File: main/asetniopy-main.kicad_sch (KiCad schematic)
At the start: 19 parts, among them J1 Conn_01x02, J2 Conn_01x02, J3 Conn_01x02, J4 Conn_01x02, J5 Conn_01x02, J6 Power/Reset, J7 BAT+, J8 BAT-, U1 ProMicro, U2 LIS2DW12

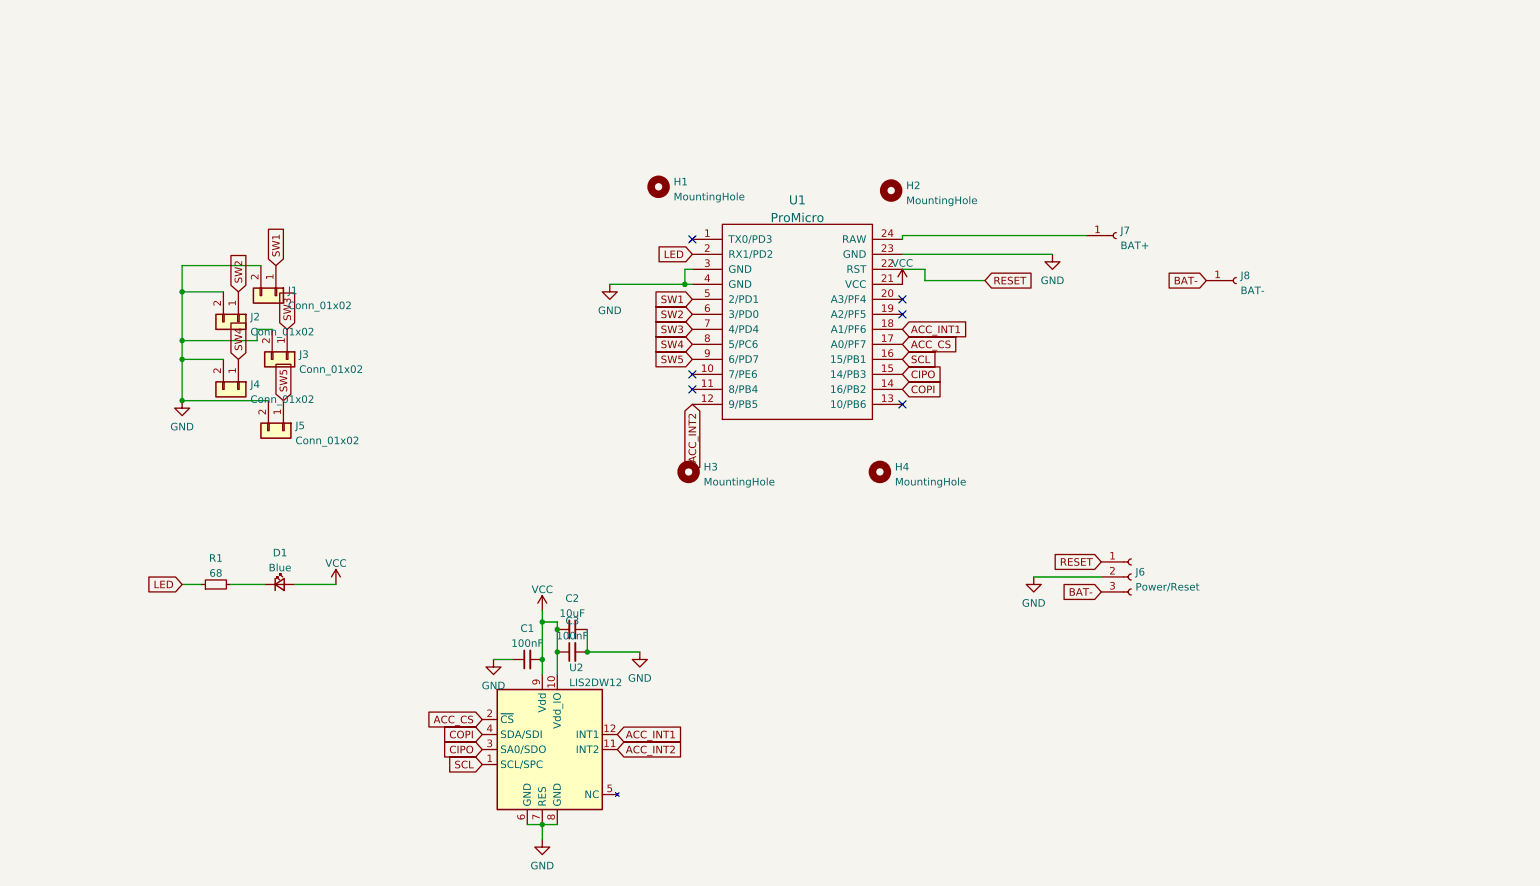
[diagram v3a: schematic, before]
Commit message: Switch to RGB LED.
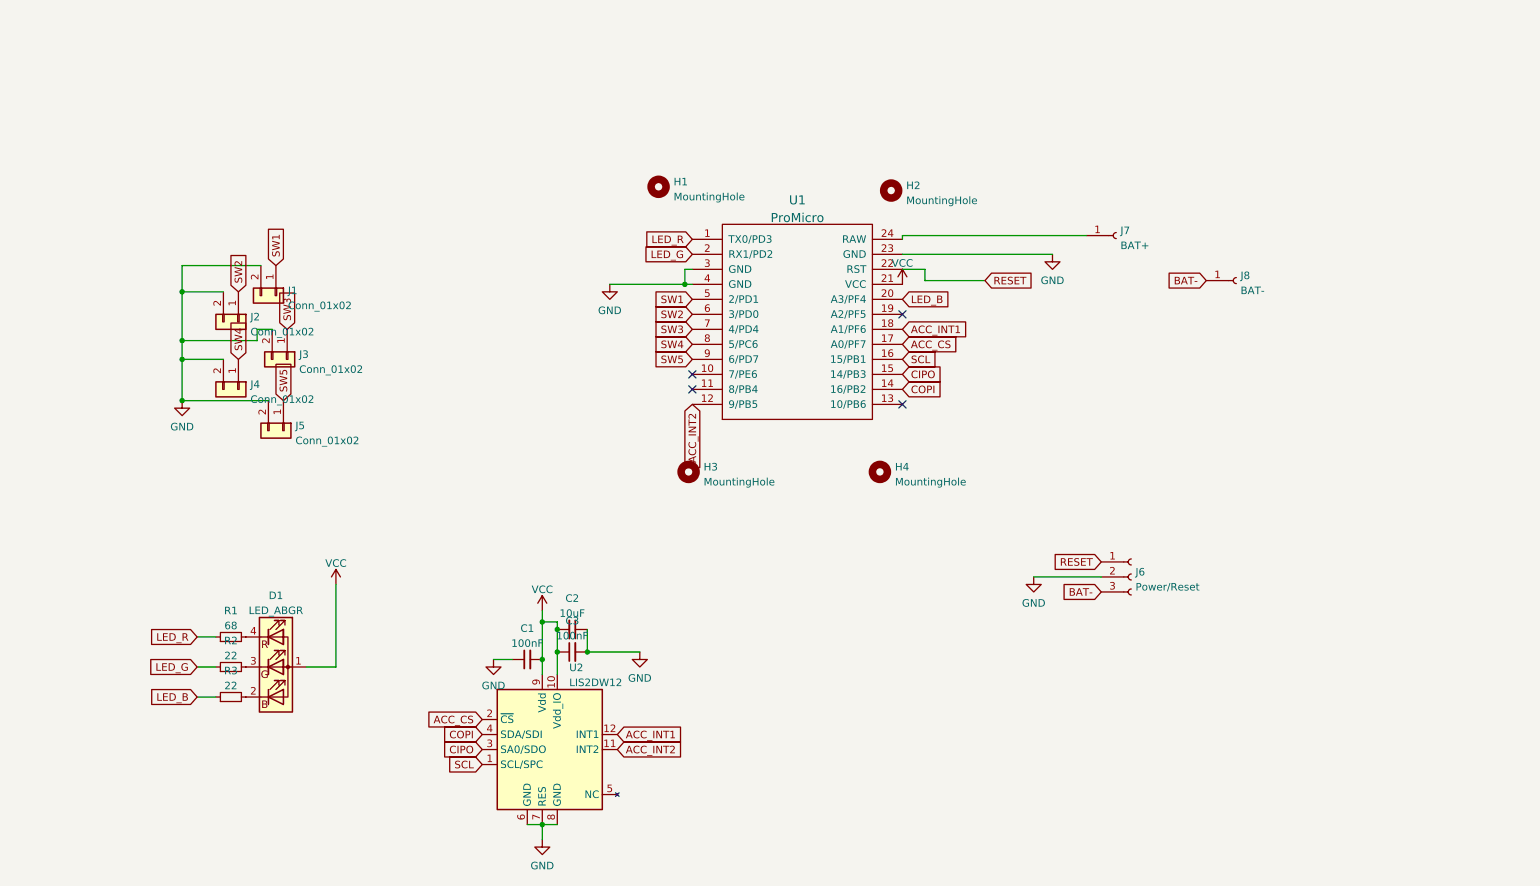
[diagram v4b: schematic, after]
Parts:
- removed D1: Blue, LED_SMD:LED_0603_1608Metric, symbol Device:LED_Small
- added D1: LED_ABGR, LED_SMD:LED_RGB_Wuerth-PLCC4_3.2x2.8mm_150141M173100, symbol Device:LED_ABGR
- added R2, R3: 22, Resistor_SMD:R_0603_1608Metric, symbol Device:R_Small
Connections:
- net VCC: now also D1.1 (A)
- net at R1.2: now also D1.4 (RK)
- net LED_R: now reaches U1.1 (TX0/PD3)
- net LED_R: now also R1.1
- net LED_B: now reaches U1.20 (A3/PF4)
- net LED_B: now also R3.1
- net LED renamed LED_G
- net LED_G: now also R2.1; no longer R1.1
- new net: D1.2 (BK), R3.2
- new net: D1.3 (GK), R2.2
- no-connect marks 6 -> 4
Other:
- moved on the sheet: R1
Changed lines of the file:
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@@
   )
   (no_connect (at 172.085 74.93))
-  (no_connect (at 136.525 62.23))
   (no_connect (at 136.525 85.09))
   (no_connect (at 136.525 87.63))
   (no_connect (at 172.085 90.17))
-  (no_connect (at 172.085 72.39))
   (wire (pts (xy 50.165 82.55) (xy 50.165 89.535))
     (stroke (width 0) (type default) (color 0 0 0 0))
@@
     (stroke (width 0) (type default) (color 0 0 0 0))
   )
+  (wire (pts (xy 76.2 120.65) (xy 76.2 134.62))
+    (stroke (width 0) (type default) (color 0 0 0 0))
+  )
   (wire (pts (xy 50.165 82.55) (xy 57.15 82.55))
     (stroke (width 0) (type default) (color 0 0 0 0))
@@
     (stroke (width 0) (type default) (color 0 0 0 0))
   )
+  (wire (pts (xy 52.705 139.7) (xy 55.88 139.7))
+    (stroke (width 0) (type default) (color 0 0 0 0))
+  )
   (wire (pts (xy 111.125 161.29) (xy 111.125 163.83))
     (stroke (width 0) (type default) (color 0 0 0 0))
@@
     (stroke (width 0) (type default) (color 0 0 0 0))
   )
+  (wire (pts (xy 52.705 134.62) (xy 55.88 134.62))
+    (stroke (width 0) (type default) (color 0 0 0 0))
+  )
   (wire (pts (xy 136.525 67.31) (xy 135.255 67.31))
     (stroke (width 0) (type default) (color 0 0 0 0))
@@
     (stroke (width 0) (type default) (color 0 0 0 0))
   )
-  (wire (pts (xy 69.215 120.65) (xy 76.2 120.65))
-    (stroke (width 0) (type default) (color 0 0 0 0))
-  )
   (wire (pts (xy 50.165 79.375) (xy 62.865 79.375))
     (stroke (width 0) (type default) (color 0 0 0 0))
@@
     (stroke (width 0) (type default) (color 0 0 0 0))
   )
-  (wire (pts (xy 50.165 120.65) (xy 53.34 120.65))
-    (stroke (width 0) (type default) (color 0 0 0 0))
-  )
-  (wire (pts (xy 58.42 120.65) (xy 64.135 120.65))
+  (wire (pts (xy 52.705 129.54) (xy 55.88 129.54))
+    (stroke (width 0) (type default) (color 0 0 0 0))
+  )
+  (wire (pts (xy 76.2 134.62) (xy 71.12 134.62))
     (stroke (width 0) (type default) (color 0 0 0 0))
   )
@@
     )
   )
+  (global_label "LED_B" (shape input) (at 52.705 139.7 180) (fields_autoplaced)
+    (effects (font (size 1.27 1.27)) (justify right))
+    (property "Intersheet References" "${INTERSHEET_REFS}" (id 0) (at 44.6071 139.6206 0)
+      (effects (font (size 1.27 1.27)) (justify right) hide)
+    )
+  )
   (global_label "BAT-" (shape input) (at 223.52 69.215 180) (fields_autoplaced)
     (effects (font (size 1.27 1.27)) (justify right))
@@
     )
   )
-  (global_label "LED" (shape input) (at 136.525 64.77 180) (fields_autoplaced)
-    (effects (font (size 1.27 1.27)) (justify right))
-    (property "Intersheet References" "${INTERSHEET_REFS}" (id 0) (at 130.6648 64.6906 0)
+  (global_label "LED_G" (shape input) (at 136.525 64.77 180) (fields_autoplaced)
+    (effects (font (size 1.27 1.27)) (justify right))
+    (property "Intersheet References" "${INTERSHEET_REFS}" (id 0) (at 128.4271 64.6906 0)
       (effects (font (size 1.27 1.27)) (justify right) hide)
     )
@@
     )
   )
+  (global_label "LED_B" (shape input) (at 172.085 72.39 0) (fields_autoplaced)
+    (effects (font (size 1.27 1.27)) (justify left))
+    (property "Intersheet References" "${INTERSHEET_REFS}" (id 0) (at 180.1829 72.3106 0)
+      (effects (font (size 1.27 1.27)) (justify left) hide)
+    )
+  )
   (global_label "SW3" (shape input) (at 136.525 77.47 180) (fields_autoplaced)
     (effects (font (size 1.27 1.27)) (justify right))
@@
     )
   )
+  (global_label "LED_R" (shape input) (at 136.525 62.23 180) (fields_autoplaced)
+    (effects (font (size 1.27 1.27)) (justify right))
+    (property "Intersheet References" "${INTERSHEET_REFS}" (id 0) (at 128.4271 62.1506 0)
+      (effects (font (size 1.27 1.27)) (justify right) hide)
+    )
+  )
+  (global_label "LED_G" (shape input) (at 52.705 134.62 180) (fields_autoplaced)
+    (effects (font (size 1.27 1.27)) (justify right))
+    (property "Intersheet References" "${INTERSHEET_REFS}" (id 0) (at 44.6071 134.5406 0)
+      (effects (font (size 1.27 1.27)) (justify right) hide)
+    )
+  )
   (global_label "SW3" (shape input) (at 67.945 77.47 90) (fields_autoplaced)
     (effects (font (size 1.27 1.27)) (justify left))
@@
     )
   )
-  (global_label "LED" (shape input) (at 50.165 120.65 180) (fields_autoplaced)
-    (effects (font (size 1.27 1.27)) (justify right))
-    (property "Intersheet References" "${INTERSHEET_REFS}" (id 0) (at 44.3048 120.7294 0)
-      (effects (font (size 1.27 1.27)) (justify right) hide)
-    )
-  )
-  (symbol (lib_id "Device:R_Small") (at 55.88 120.65 90) (unit 1)
-    (in_bom yes) (on_board yes) (fields_autoplaced)
-    (property "Reference" "R1" (id 0) (at 55.88 116.2136 90))
-    (property "Value" "68" (id 1) (at 55.88 118.7505 90))
-    (property "Footprint" "Resistor_SMD:R_0603_1608Metric" (id 2) (at 55.88 120.65 0)
-      (effects (font (size 1.27 1.27)) hide)
-    )
-    (property "Datasheet" "~" (id 3) (at 55.88 120.65 0)
-      (effects (font (size 1.27 1.27)) hide)
-    )
-    (property "LCSC Part Number" "C27592" (id 4) (at 55.88 120.65 90)
+  (global_label "LED_R" (shape input) (at 52.705 129.54 180) (fields_autoplaced)
+    (effects (font (size 1.27 1.27)) (justify right))
+    (property "Intersheet References" "${INTERSHEET_REFS}" (id 0) (at 44.6071 129.4606 0)
+      (effects (font (size 1.27 1.27)) (justify right) hide)
+    )
+  )
+  (symbol (lib_id "Device:R_Small") (at 58.42 129.54 90) (unit 1)
+    (in_bom yes) (on_board yes) (fields_autoplaced)
+    (property "Reference" "R1" (id 0) (at 58.42 125.1036 90))
+    (property "Value" "68" (id 1) (at 58.42 127.6405 90))
+    (property "Footprint" "Resistor_SMD:R_0603_1608Metric" (id 2) (at 58.42 129.54 0)
+      (effects (font (size 1.27 1.27)) hide)
+    )
+    (property "Datasheet" "~" (id 3) (at 58.42 129.54 0)
+      (effects (font (size 1.27 1.27)) hide)
+    )
+    (property "LCSC Part Number" "C27592" (id 4) (at 58.42 129.54 90)
       (effects (font (size 1.27 1.27)) hide)
     )
@@
       (effects (font (size 1.27 1.27)) hide)
     )
+  )
+  (symbol (lib_id "Device:R_Small") (at 58.42 139.7 90) (unit 1)
+    (in_bom yes) (on_board yes) (fields_autoplaced)
+    (property "Reference" "R3" (id 0) (at 58.42 135.2636 90))
+    (property "Value" "22" (id 1) (at 58.42 137.8005 90))
+    (property "Footprint" "Resistor_SMD:R_0603_1608Metric" (id 2) (at 58.42 139.7 0)
+      (effects (font (size 1.27 1.27)) hide)
+    )
+    (property "Datasheet" "~" (id 3) (at 58.42 139.7 0)
+      (effects (font (size 1.27 1.27)) hide)
+    )
+    (property "LCSC Part Number" "C25092" (id 4) (at 58.42 139.7 90)
+      (effects (font (size 1.27 1.27)) hide)
+    )
+    (pin "1")
+    (pin "2")
   )
   (symbol (lib_id "power:VCC") (at 76.2 120.65 0) (unit 1)
@@
     (pin "9")
   )
+  (symbol (lib_id "Device:LED_ABGR") (at 66.04 134.62 0) (unit 1)
+    (in_bom yes) (on_board yes) (fields_autoplaced)
+    (property "Reference" "D1" (id 0) (at 66.04 122.5382 0))
+    (property "Value" "LED_ABGR" (id 1) (at 66.04 125.0751 0))
+    (property "Footprint" "LED_SMD:LED_RGB_Wuerth-PLCC4_3.2x2.8mm_150141M173100" (id 2) (at 66.04 135.89 0)
+      (effects (font (size 1.27 1.27)) hide)
+    )
+    (property "Datasheet" "~" (id 3) (at 66.04 135.89 0)
+      (effects (font (size 1.27 1.27)) hide)
+    )
+    (property "LCSC Part Number" "C409779" (id 4) (at 66.04 134.62 0)
+      (effects (font (size 1.27 1.27)) hide)
+    )
+    (pin "1")
+    (pin "2")
+    (pin "3")
+    (pin "4")
+  )
   (symbol (lib_id "power:GND") (at 50.165 89.535 0) (unit 1)
     (in_bom yes) (on_board yes) (fields_autoplaced)
@@
       (effects (font (size 1.27 1.27)) hide)
     )
-  )
-  (symbol (lib_id "Device:LED_Small") (at 66.675 120.65 0) (unit 1)
-    (in_bom yes) (on_board yes) (fields_autoplaced)
-    (property "Reference" "D1" (id 0) (at 66.7385 115.2992 0))
-    (property "Value" "Blue" (id 1) (at 66.7385 117.8361 0))
-    (property "Footprint" "LED_SMD:LED_0603_1608Metric" (id 2) (at 66.675 120.65 90)
-      (effects (font (size 1.27 1.27)) hide)
-    )
-    (property "Datasheet" "~" (id 3) (at 66.675 120.65 90)
-      (effects (font (size 1.27 1.27)) hide)
-    )
-    (property "LCSC Part Number" "C72041" (id 4) (at 66.675 120.65 0)
-      (effects (font (size 1.27 1.27)) hide)
-    )
-    (pin "1")
-    (pin "2")
   )
   (symbol (lib_id "Device:C_Small") (at 108.585 133.35 90) (unit 1)
@@
     (pin "1")
   )
+  (symbol (lib_id "Device:R_Small") (at 58.42 134.62 90) (unit 1)
+    (in_bom yes) (on_board yes) (fields_autoplaced)
+    (property "Reference" "R2" (id 0) (at 58.42 130.1836 90))
+    (property "Value" "22" (id 1) (at 58.42 132.7205 90))
+    (property "Footprint" "Resistor_SMD:R_0603_1608Metric" (id 2) (at 58.42 134.62 0)
+      (effects (font (size 1.27 1.27)) hide)
+    )
+    (property "Datasheet" "~" (id 3) (at 58.42 134.62 0)
+      (effects (font (size 1.27 1.27)) hide)
+    )
+    (property "LCSC Part Number" "C25092" (id 4) (at 58.42 134.62 90)
+      (effects (font (size 1.27 1.27)) hide)
+    )
+    (pin "1")
+    (pin "2")
+  )
   (sheet_instances
     (path "/" (page "1"))
@@
       (reference "C3") (unit 1) (value "100nF") (footprint "Capacitor_SMD:C_0603_1608Metric")
     )
-    (path "/a3912c3b-a7ed-4069-b82c-93c869bd3701"
-      (reference "D1") (unit 1) (value "Blue") (footprint "LED_SMD:LED_0603_1608Metric")
+    (path "/6aa44c90-40ff-48d0-a20c-c2bf3cc0eac1"
+      (reference "D1") (unit 1) (value "LED_ABGR") (footprint "LED_SMD:LED_RGB_Wuerth-PLCC4_3.2x2.8mm_150141M173100")
     )
     (path "/9d3116ed-06f0-4c20-9f12-ed2bc968344c"
@@
       (reference "R1") (unit 1) (value "68") (footprint "Resistor_SMD:R_0603_1608Metric")
     )
+    (path "/fd481f99-4b83-4550-96b3-82f440b2ee40"
+      (reference "R2") (unit 1) (value "22") (footprint "Resistor_SMD:R_0603_1608Metric")
+    )
+    (path "/244a0153-1764-421a-a31b-f6dc454193e1"
+      (reference "R3") (unit 1) (value "22") (footprint "Resistor_SMD:R_0603_1608Metric")
+    )
     (path "/68a8640f-4b2f-4c4c-a0f5-e46c810f4f86"

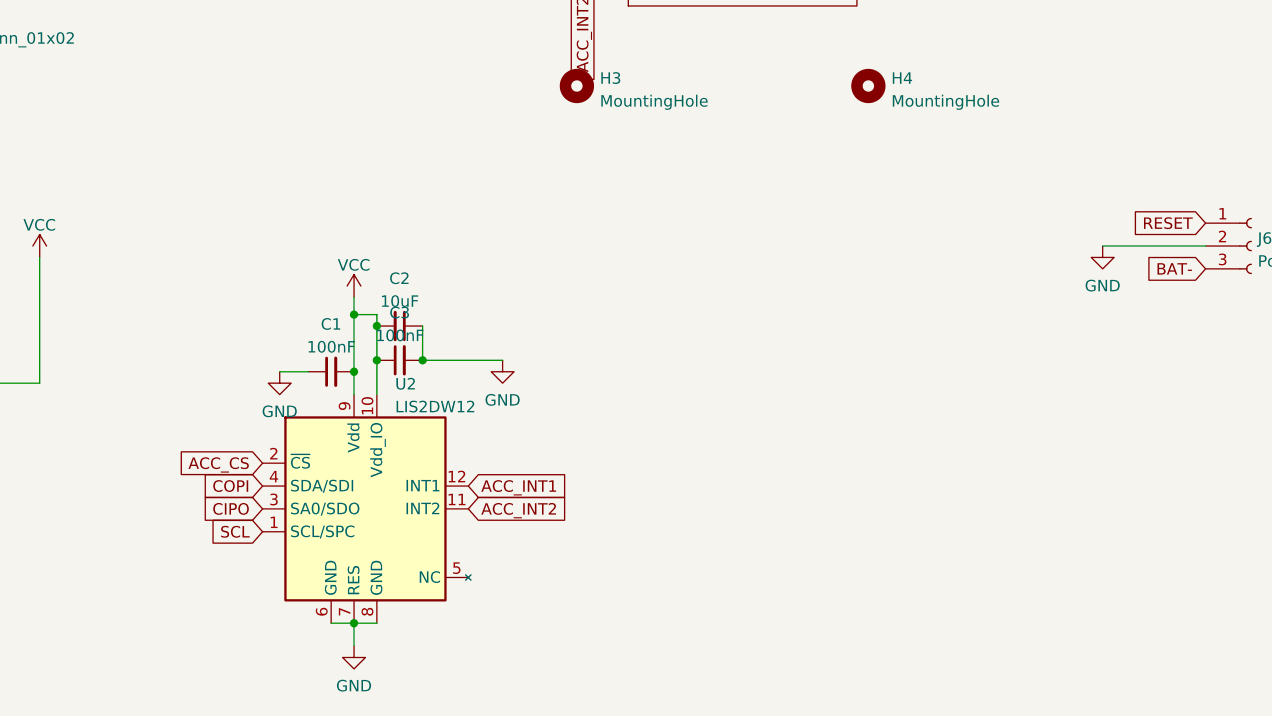
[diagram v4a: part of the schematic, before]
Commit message: Move to LSM6DSO iNEMO IC.
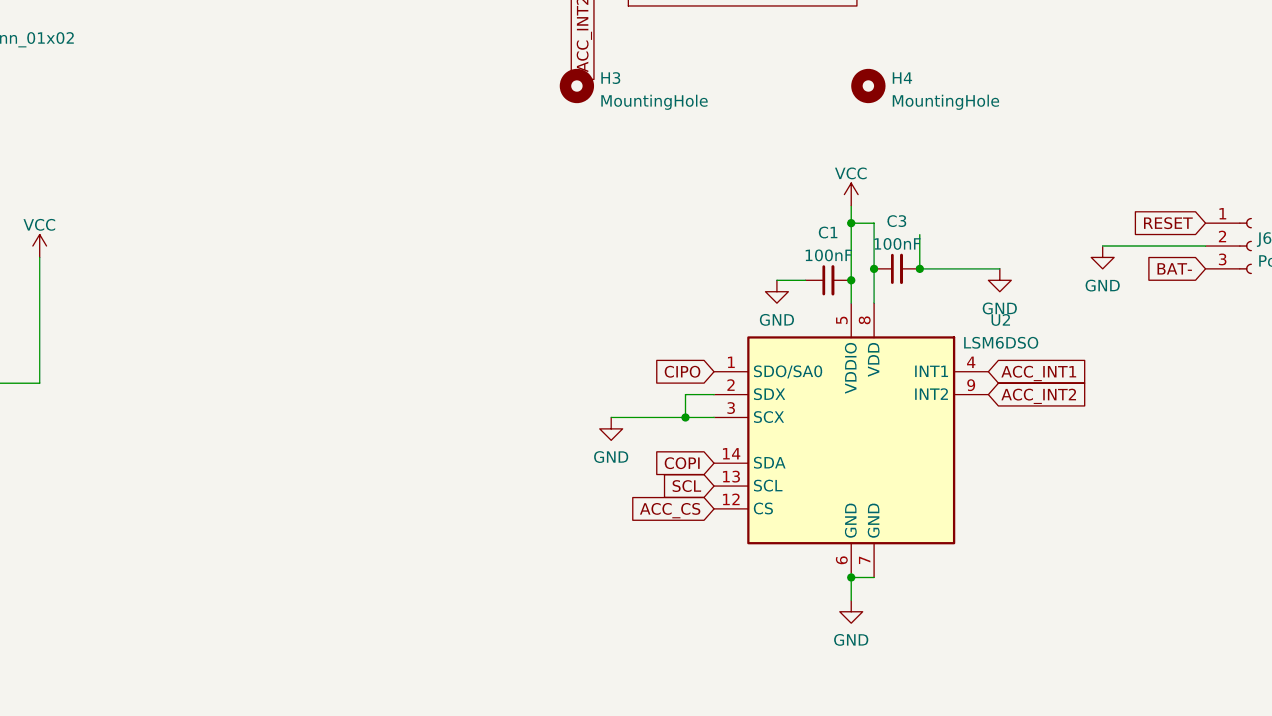
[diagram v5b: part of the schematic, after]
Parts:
- removed C2: 10uF, Capacitor_Tantalum_SMD:CP_EIA-3216-18_Kemet-A, symbol Device:C_Small
- removed U2: LIS2DW12, Package_LGA:LGA-12_2x2mm_P0.5mm, symbol lis2dw12:LIS2DW12
- added U2: LSM6DSO, main:PQFN50P250X300X86-14N, symbol Sensor_Motion:LSM6DS3
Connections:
- net ACC_CS: now also U2.12 (CS)
- net ACC_INT1: now also U2.4 (INT1)
- net ACC_INT2: now also U2.9 (INT2)
- net CIPO: now also U2.1 (SDO/SA0)
- net COPI: now also U2.14 (SDA)
- net GND: now also U2.2 (SDX), U2.3 (SCX), U2.6 (GND), U2.7 (GND)
- net SCL: now also U2.13 (SCL)
- net VCC: now also U2.5 (VDDIO), U2.8 (VDD)
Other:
- moved on the sheet: C1, C3
